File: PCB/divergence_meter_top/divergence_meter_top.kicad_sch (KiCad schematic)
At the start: 11 parts

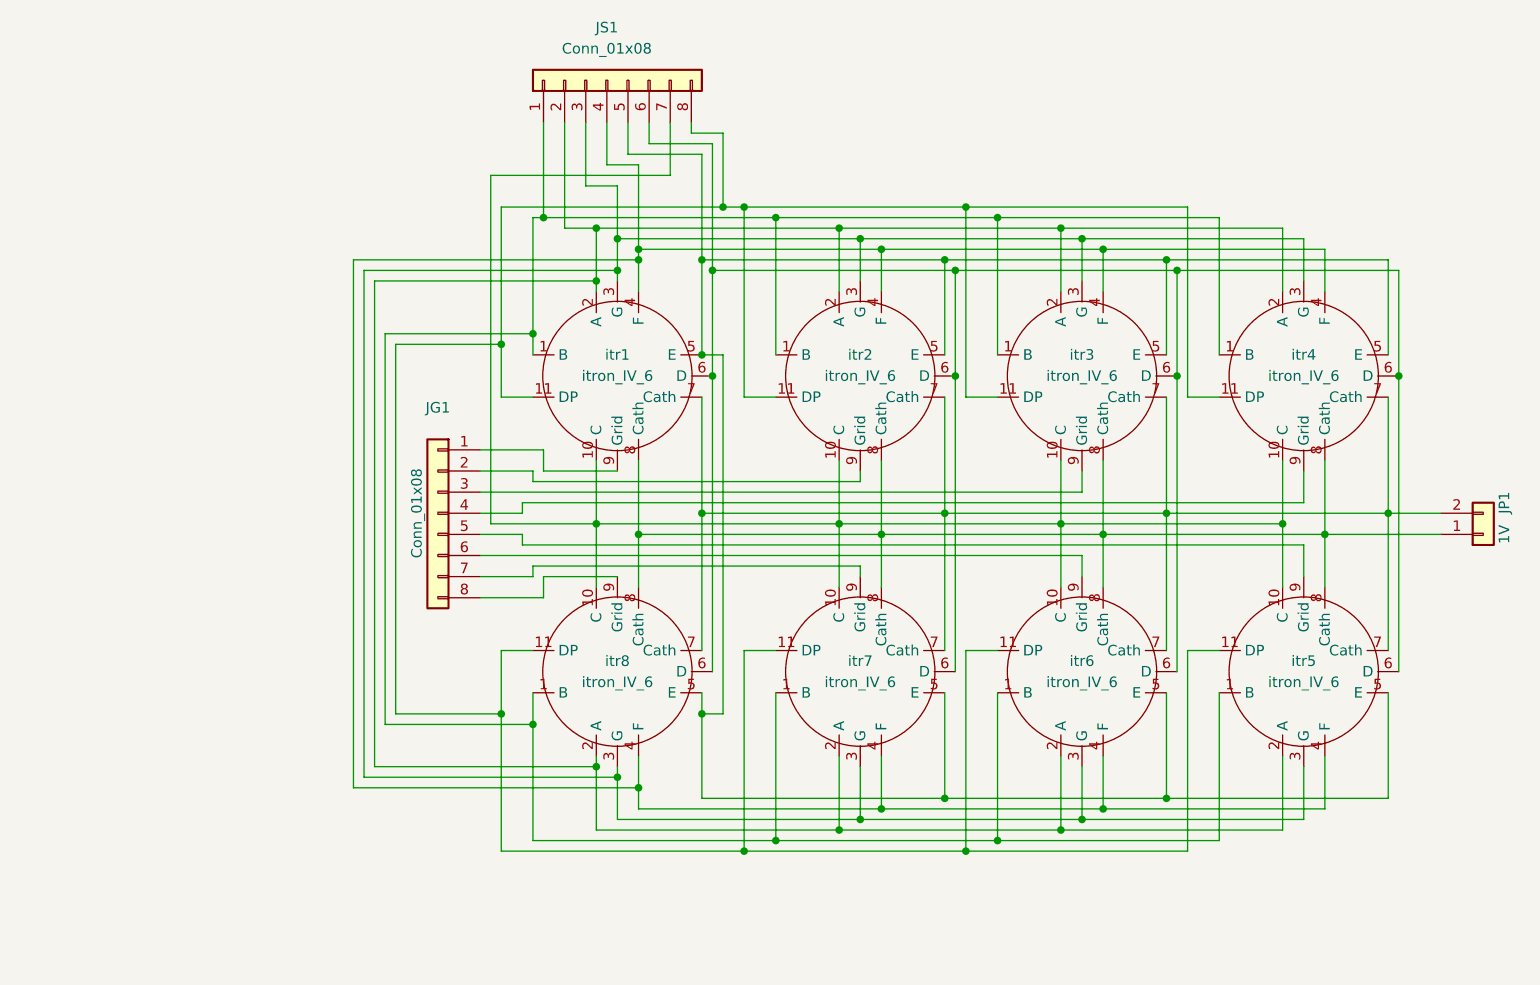
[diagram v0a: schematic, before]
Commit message: logic pcb almost finished, remaking top
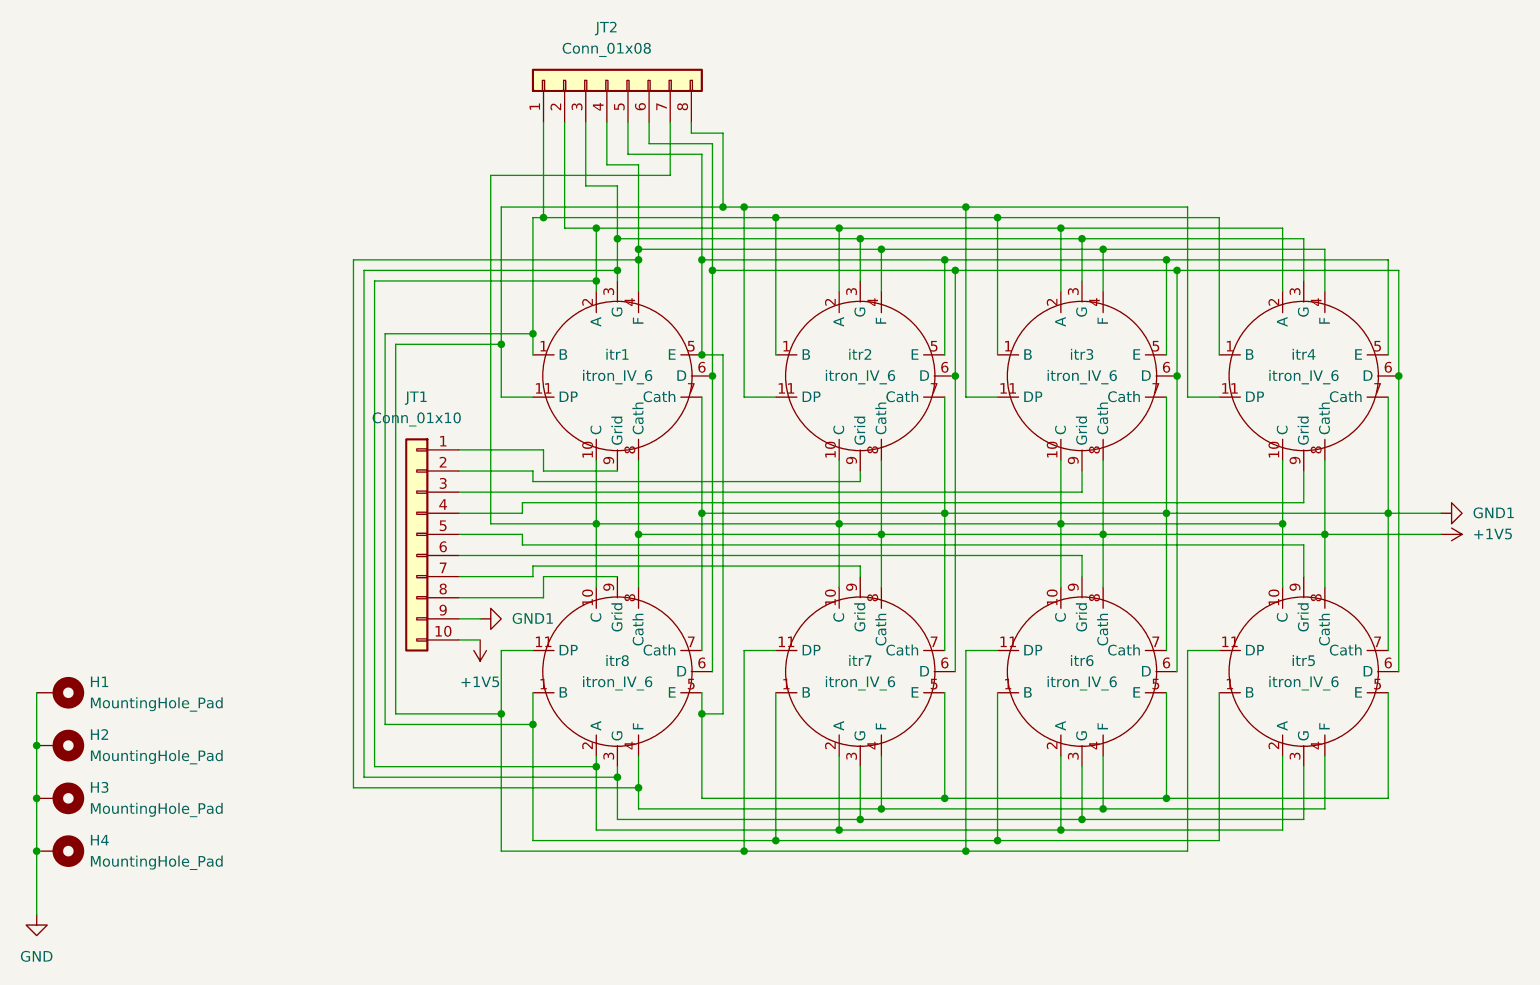
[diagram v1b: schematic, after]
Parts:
- removed JG1: Conn_01x08, Connector_PinHeader_2.54mm:PinHeader_1x08_P2.54mm_Vertical, symbol Connector_Generic:Conn_01x08
- removed JP1: 1V, Connector_PinHeader_2.54mm:PinHeader_1x02_P2.54mm_Vertical, symbol Connector_Generic:Conn_01x02
- added H1, H2, H3, H4: MountingHole_Pad, MountingHole:MountingHole_3.5mm_Pad_Via, symbol Mechanical:MountingHole_Pad
- added JT1: Conn_01x10, Connector_PinHeader_2.54mm:PinHeader_1x10_P2.54mm_Vertical, symbol Connector_Generic:Conn_01x10
- renumbered JS1 to JT2
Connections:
- net GND1: now reaches itr1.7 (Cath), itr2.7 (Cath), itr3.7 (Cath), itr4.7 (Cath), itr5.7 (Cath), itr6.7 (Cath), itr7.7 (Cath), itr8.7 (Cath)
- net GND1: now also JT1.9 (Pin_9)
- net +1V5: now reaches itr1.8 (Cath), itr2.8 (Cath), itr3.8 (Cath), itr4.8 (Cath), itr5.8 (Cath), itr6.8 (Cath), itr7.8 (Cath), itr8.8 (Cath)
- net +1V5: now also JT1.10 (Pin_10)
- net at itr1.9 (Grid): now also JT1.1 (Pin_1)
- net at itr6.9 (Grid): now also JT1.6 (Pin_6)
- net at itr4.9 (Grid): now also JT1.4 (Pin_4)
- net at itr2.9 (Grid): now also JT1.2 (Pin_2)
- net at itr3.9 (Grid): now also JT1.3 (Pin_3)
- net at itr5.9 (Grid): now also JT1.5 (Pin_5)
- net at itr7.9 (Grid): now also JT1.7 (Pin_7)
- net at itr8.9 (Grid): now also JT1.8 (Pin_8)
- new net GND: H1.1, H2.1, H3.1, H4.1

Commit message: PCB done, exported gerber
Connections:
- net GND renamed Earth
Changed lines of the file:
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@@
+    (pin "1")
+  )
+  (symbol (lib_id "power:Earth") (at 53.34 148.59 0) (unit 1)
+    (in_bom yes) (on_board yes) (fields_autoplaced)
+    (property "Reference" "#PWR?" (id 0) (at 53.34 154.94 0)
+      (effects (font (size 1.27 1.27)) hide)
+    )
+    (property "Value" "Earth" (id 1) (at 53.34 152.4 0)
+      (effects (font (size 1.27 1.27)) hide)
+    )
+    (property "Footprint" "" (id 2) (at 53.34 148.59 0)
+      (effects (font (size 1.27 1.27)) hide)
+    )
+    (property "Datasheet" "~" (id 3) (at 53.34 148.59 0)
+      (effects (font (size 1.27 1.27)) hide)
+    )
     (pin "1")
   )
@@
     (pin "9")
   )
-  (symbol (lib_id "power:GND") (at 53.34 148.59 0) (unit 1)
-    (in_bom yes) (on_board yes) (fields_autoplaced)
-    (property "Reference" "#PWR01" (id 0) (at 53.34 154.94 0)
-      (effects (font (size 1.27 1.27)) hide)
-    )
-    (property "Value" "GND" (id 1) (at 53.34 153.67 0))
-    (property "Footprint" "" (id 2) (at 53.34 148.59 0)
-      (effects (font (size 1.27 1.27)) hide)
-    )
-    (property "Datasheet" "" (id 3) (at 53.34 148.59 0)
-      (effects (font (size 1.27 1.27)) hide)
-    )
-    (pin "1")
-  )
   (symbol (lib_id "itron_iv_6:itron_IV_6") (at 152.4 133.35 0) (mirror x) (unit 1)
     (in_bom yes) (on_board yes)
@@
   )
   (symbol_instances
-    (path "/e9d6d87a-0c45-42d5-b43b-38b2b19f6b19"
-      (reference "#PWR01") (unit 1) (value "GND") (footprint "")
-    )
     (path "/b179022b-e294-47d5-9357-618f8dfa1093"
       (reference "#PWR0101") (unit 1) (value "GND1") (footprint "")
@@
       (reference "#PWR0104") (unit 1) (value "+1V5") (footprint "")
     )
+    (path "/c399aef9-3678-4747-9295-3eabdcc57d0c"
+      (reference "#PWR?") (unit 1) (value "Earth") (footprint "")
+    )
     (path "/959049d5-8131-4d90-90cb-f74b567fc392"
